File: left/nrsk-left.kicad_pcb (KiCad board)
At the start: 2 copper layers, 179.9 x 132.5 mm, 139 parts, among them J1 PJ-320D, J2 USB-C, J3 OLED 128x32, SW1 Esc, SW10 1, SW11 2, SW12 3, SW13 4, SW14 5, SW15 6, SW16 16, SW17 Tab, SW18 Q, SW19 W, SW2 F1, SW20 E, SW21 R, SW22 T, SW23 23, SW24 Ctrl, SW25 A, SW26 S, SW27 D, SW28 F, SW29 G, SW3 F2, SW30 30, SW31 Shift, SW32 Z, SW33 X, SW34 C, SW35 V, SW36 B, SW37 37, SW38 Ctrl, SW39 Opt, SW4 F3, SW40 Cmd, SW41 Space, SW42 Space, SW43 Space, SW44 44, SW5 F4, SW6 F5, SW7 F6, SW8 8, SW9 `, U1 RP2040, U2 USBLC6-2SC6, U3 AS5600-ASOM, U4 AP2112K-3.3, U5 W25Q128JVS, Y1 12MHz

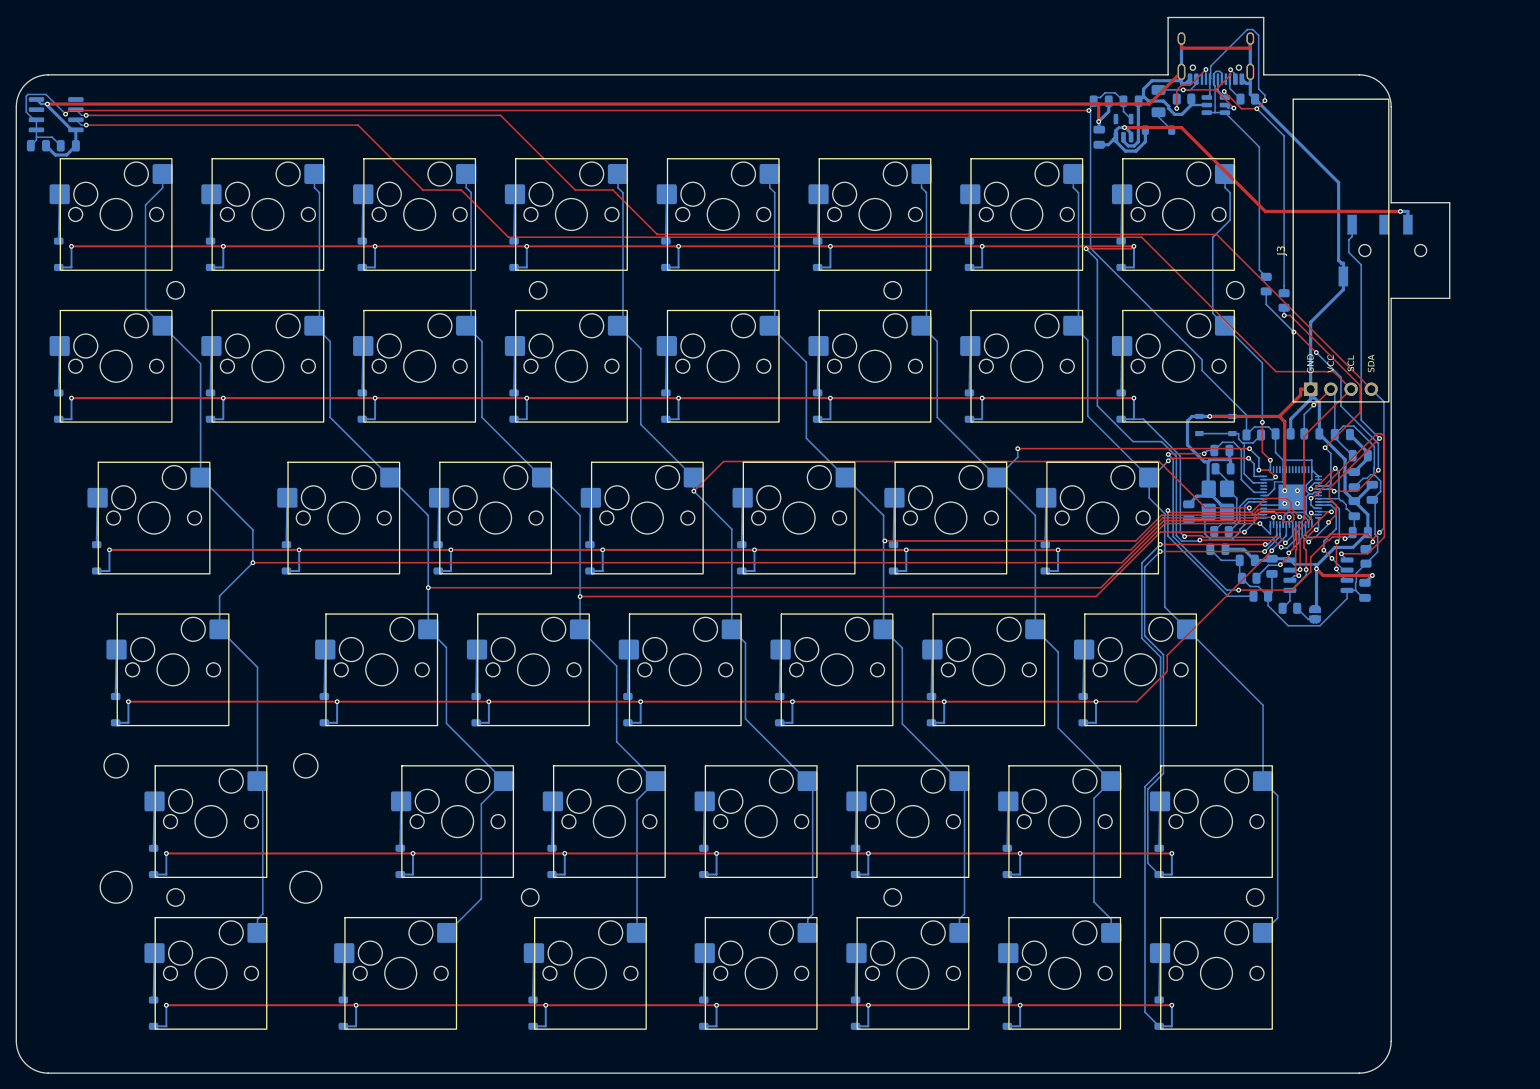
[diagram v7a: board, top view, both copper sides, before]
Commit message: TRRS on the top edge next to USB-C; rounded tongues; B lid fillet; keycap legends
- Both connectors on the back edge (TRRS 17 mm from the inner edge, USB-C 18 mm further out); boards re-routed
- Tongue tips R2.5, roots R1.5 on Edge.Cuts
- Shared port cap when the two ports sit close together
- All-printed plate: R1 on the top outer edge
- Blender renders: keycap legends; refreshed A/B, ports and wheel images

Co-Authored-By: Claude Opus 5.5 <noreply@anthropic.com>
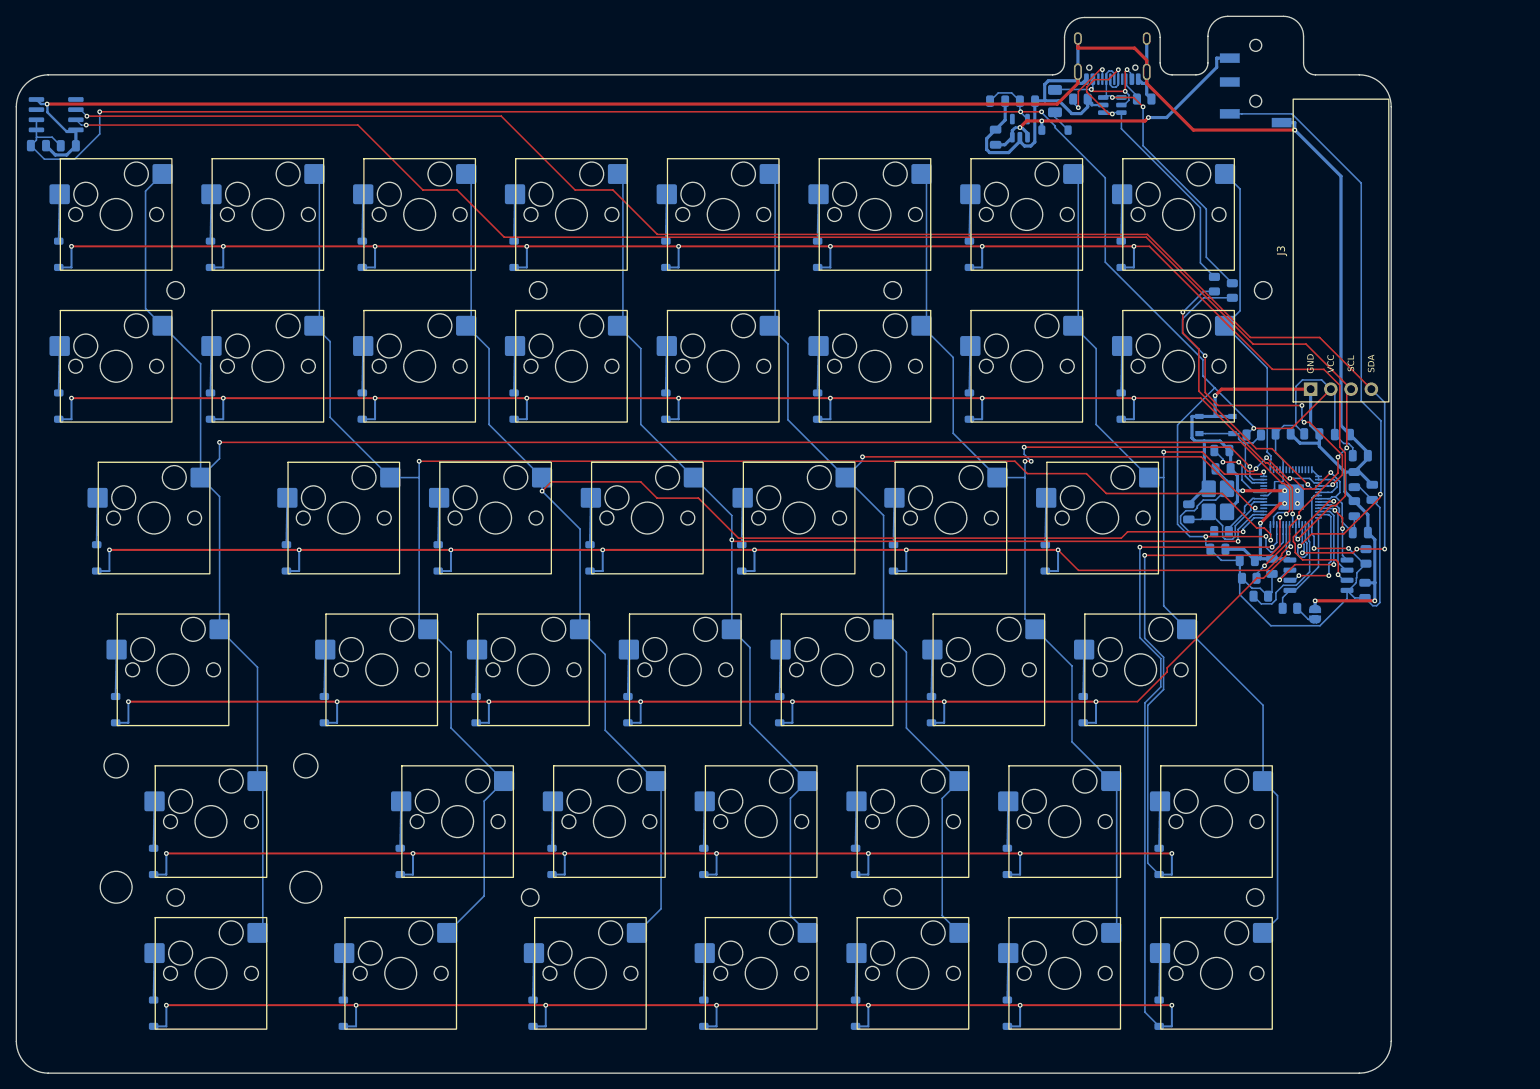
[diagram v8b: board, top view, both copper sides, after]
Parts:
- moved J1 26.3 mm to (182.6, 23.1), turned to -90 degrees
- moved C16 13.0 mm to (149.9, 29.8)
- moved C17 13.0 mm to (153.9, 25.3)
- moved C19 13.0 mm to (150.2, 25.3)
- moved D99 13.0 mm to (157.4, 28.9)
- moved F1 13.0 mm to (157.4, 25.3)
- moved J2 13.0 mm to (164.6, 18.5)
- moved R4 13.0 mm to (160.6, 25.0)
- moved R5 13.0 mm to (168.6, 25.0)
- moved U2 13.0 mm to (164.6, 25.8)
- moved U4 13.0 mm to (153.0, 28.7)
- moved R3 6.62 mm to (179.6, 49.1)
- moved R2 6.50 mm to (177.4, 48.3)
- moved H4 3.50 mm to (183.5, 49.0)
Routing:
- net /3V3: track 318.2 -> 367.1 mm, vias 3 -> 8
- net /1V1: track 75.0 -> 42.3 mm
- net /DATA: track 47.7 -> 79.7 mm
- net /QSPI_SD0: track 34.6 -> 9.04 mm
- net /HAND: track 37.6 -> 15.6 mm, vias 2 -> 0
- net GND: track 390.4 -> 407.9 mm, vias 9 -> 11
- net /USB_D-: track 55.3 -> 38.3 mm, vias 3 -> 2
- net VCC: track 54.3 -> 38.0 mm, vias 2 -> 3
- net /D-: track 30.3 -> 45.4 mm, vias 2 -> 4
- net /COL0: track 237.3 -> 250.8 mm
- net /USB_D+: track 31.9 -> 41.6 mm, vias 0 -> 2
- net /ROW0: track 234.3 -> 224.7 mm, vias 11 -> 9
- net /QSPI_SD3: track 12.7 -> 19.8 mm
- net /COL1: track 219.4 -> 226.1 mm
- net /QSPI_SD2: track 12.1 -> 17.8 mm
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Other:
- board size 179.9 x 132.5 mm -> 172.6 x 132.6 mm
